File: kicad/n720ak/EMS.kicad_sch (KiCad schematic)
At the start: 2 parts, among them J501 SV-EMS-220 DB37, J502 MZ-30

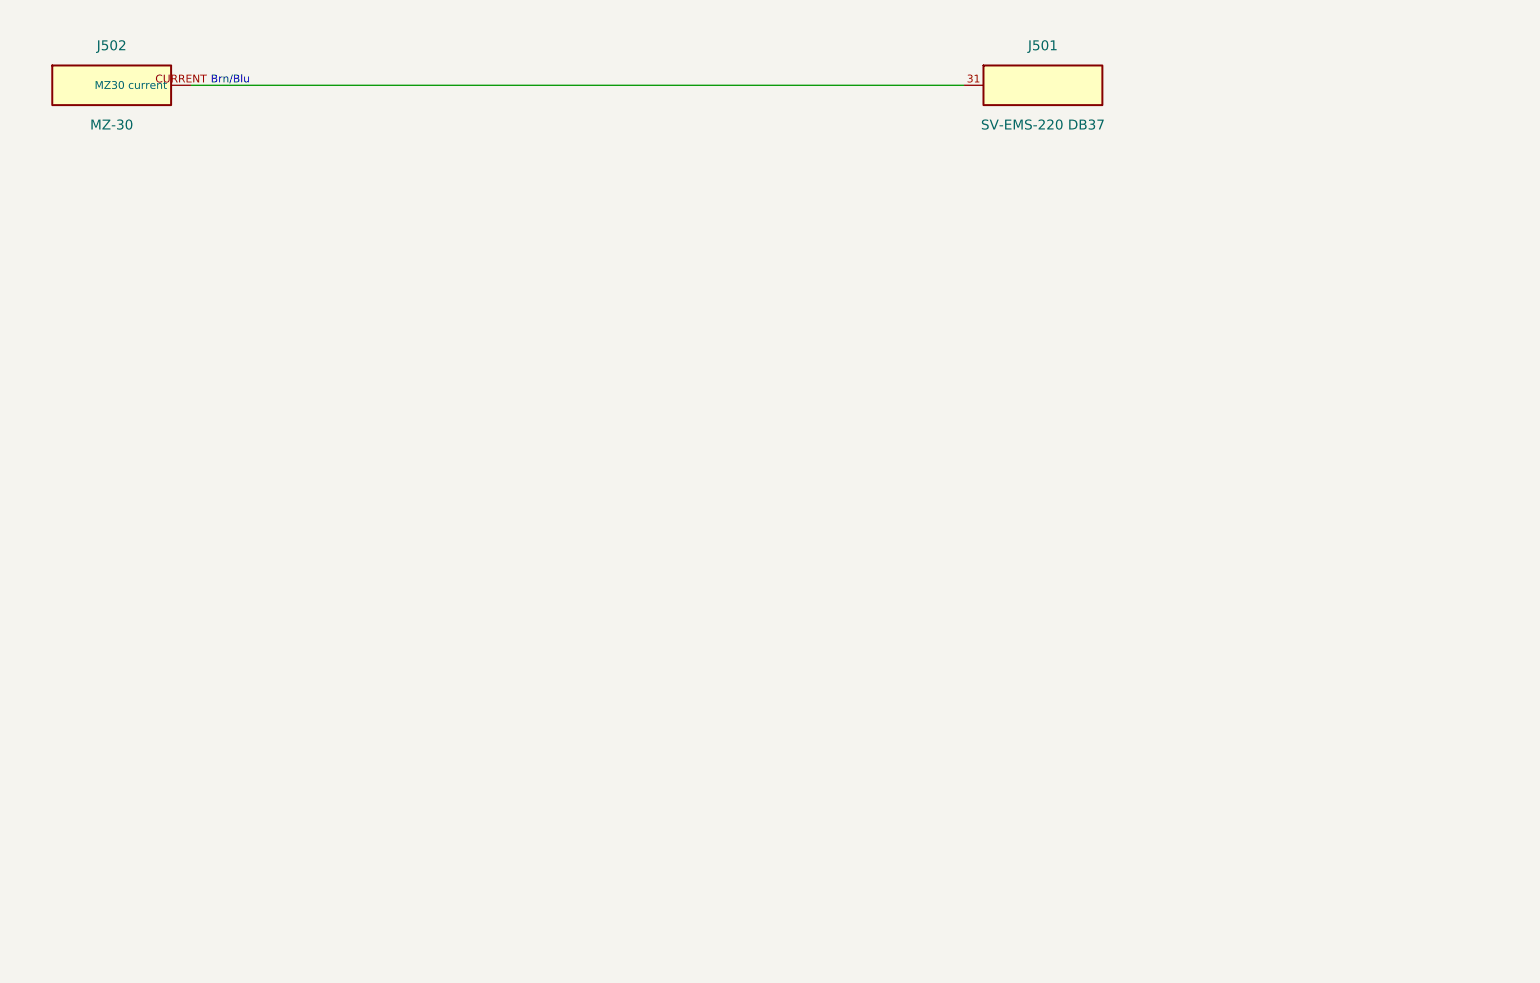
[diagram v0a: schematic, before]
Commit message: Build wing, terminal-block and EMS wire lists from the handbook tables
The wings, the under-seat terminal blocks and the EMS-220's 37-pin connector
are on no SteinAir drawing. Their only record is the owner's typed build
notes in sys-24 and sys-33. scripts/wirelist_handbook.py reads those tables
directly, so the WING and EMS wire lists cannot drift from the handbook.
Every join across connectors records what it rests on: matching bundle and
colour, a function named at both ends, or a manufacturer colour code (Dynon
servo pigtail, Ray Allen trim sensor leads). A join none of those settles
is flagged with the question that would settle it.

- KiCad: new WING sheet, full EMS sheet. The project netlist is now verified
  as a whole, which proves the cross-sheet labels merge (EMS pin 10 reaches
  the roll trim sensor through TB-L 3 and wing-root pin 12)
- INSPECT.md groups rows by question and picks up "Confirm at inspection"
  notes: 14 items
- SV trim motor outputs become labels that join TB-L on the WING sheet
- changes.tsv: CO detector RMA replacement (452-101-012, Dec 2025), its EFIS
  wire on EMS 31 and that wire's removal; C011 now names MZ-30 output Molex
  pin 5, 2026-03
- sys-33: AeroSun Vx colour table corrected to the Rev C manual (blue =
  taxi, yellow = wig-wag, green = sync), which matches TB-R 3's green pair
- sys-24: EMS pins 36/37 added to the unused table

Co-Authored-By: Claude Opus 5.5 <noreply@anthropic.com>
Claude-Session: https://claude.ai/code/session_015SpGdnvPFhutgEDurpngu2
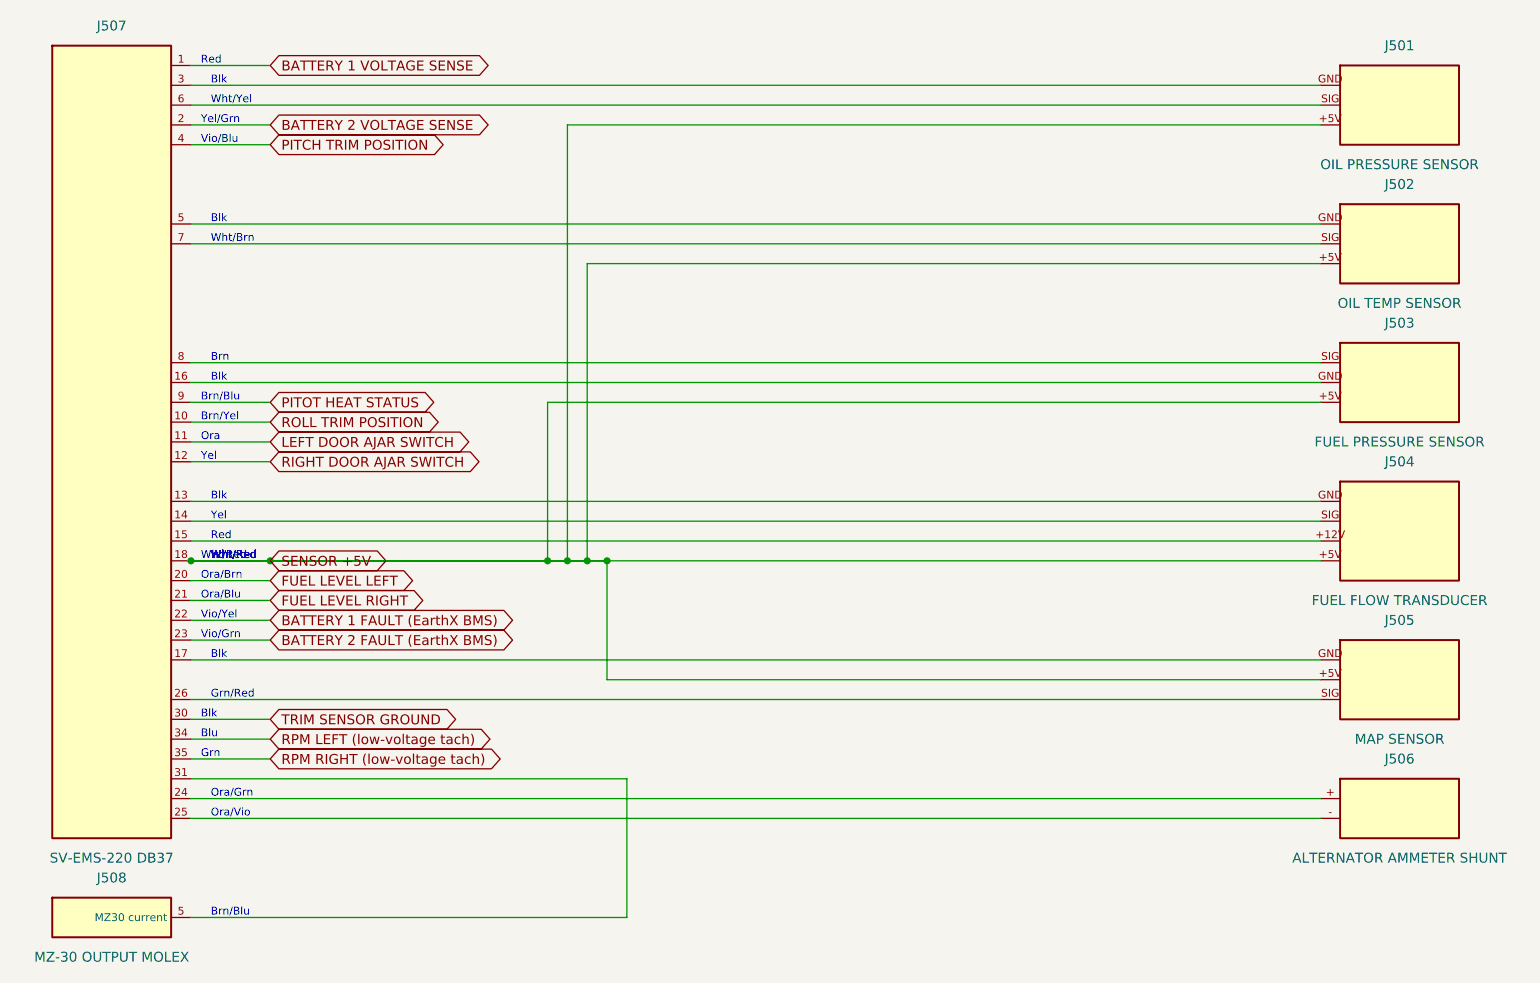
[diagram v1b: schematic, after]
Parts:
- added J503: FUEL PRESSURE SENSOR, symbol n720ak:FUEL_PRESSURE_SENSOR
- added J504: FUEL FLOW TRANSDUCER, symbol n720ak:FUEL_FLOW_TRANSDUCER
- added J505: MAP SENSOR, symbol n720ak:MAP_SENSOR
- added J506: ALTERNATOR AMMETER SHUNT, symbol n720ak:ALTERNATOR_AMMETER_SHUNT
- added J507: SV-EMS-220 DB37, symbol n720ak:SV-EMS-220_DB37
- added J508: MZ-30 OUTPUT MOLEX, symbol n720ak:MZ-30_OUTPUT_MOLEX
- J501: value SV-EMS-220 DB37 -> OIL PRESSURE SENSOR; symbol n720ak:SV-EMS-220_DB37 -> n720ak:OIL_PRESSURE_SENSOR
- J502: value MZ-30 -> OIL TEMP SENSOR; symbol n720ak:MZ-30 -> n720ak:OIL_TEMP_SENSOR
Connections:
- new net: J504.GND, J507.13
- new net: J504.SIG, J507.14
- new net: J504.+12V, J507.15
- new net: J503.GND, J507.16
- new net: J505.GND, J507.17
- new net: J506.+, J507.24
- new net: J506.-, J507.25
- new net: J505.SIG, J507.26
- new net: J501.GND, J507.3
- new net: J507.31, J508.5 (MZ30 current)
- new net: J502.GND, J507.5
- new net: J501.SIG, J507.6
- new net: J502.SIG, J507.7
- new net: J503.SIG, J507.8
- new net BATTERY 1 FAULT (EarthX BMS): J507.22
- new net BATTERY 1 VOLTAGE SENSE: J507.1
- new net BATTERY 2 FAULT (EarthX BMS): J507.23
- new net BATTERY 2 VOLTAGE SENSE: J507.2
- new net FUEL LEVEL LEFT: J507.20
- new net FUEL LEVEL RIGHT: J507.21
- new net LEFT DOOR AJAR SWITCH: J507.11
- new net PITCH TRIM POSITION: J507.4
- new net PITOT HEAT STATUS: J507.9
- new net RIGHT DOOR AJAR SWITCH: J507.12
- new net ROLL TRIM POSITION: J507.10
- new net RPM LEFT (low-voltage tach): J507.34
- new net RPM RIGHT (low-voltage tach): J507.35
- new net SENSOR +5V: J501.+5V, J502.+5V, J503.+5V, J504.+5V, J505.+5V, J507.18
- new net TRIM SENSOR GROUND: J507.30
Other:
- note added: "Blk"
- note added: "Blu"
- note added: "Brn"
- note added: "Brn/Yel"
- note added: "Grn"
- note added: "Grn/Red"
- note added: "Ora"
- note added: "Ora/Blu"
- note added: "Ora/Brn"
- note added: "Ora/Grn"
- note added: "Ora/Vio"
- note added: "Red"
- note added: "Vio/Blu"
- note added: "Vio/Grn"
- note added: "Vio/Yel"
- note added: "Wht/Brn"
- note added: "Wht/Red"
- note added: "Wht/Yel"
- note added: "Yel"
- note added: "Yel/Grn"
